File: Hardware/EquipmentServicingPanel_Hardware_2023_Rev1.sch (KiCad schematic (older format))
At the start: 42 parts, among them U1 Raspberry_Pi, U2 OKI, U3 TSR_1-2450

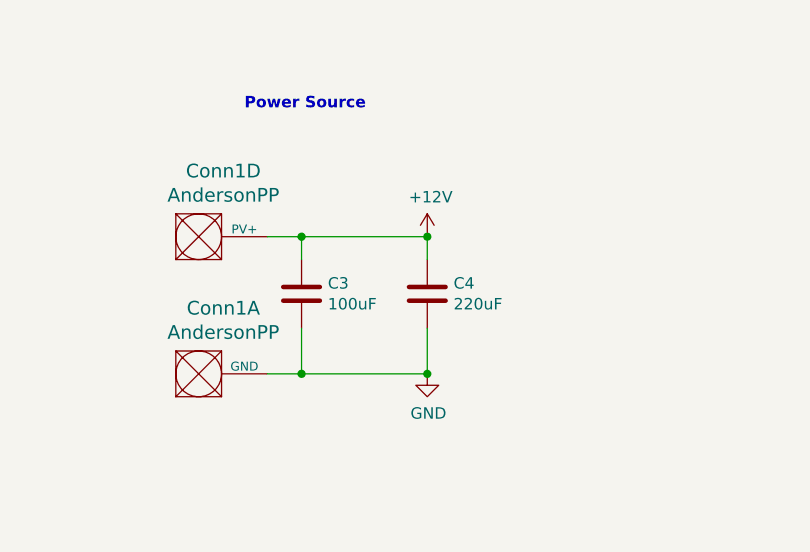
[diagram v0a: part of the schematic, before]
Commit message: Revert "Applied Kicad footprints"
This reverts commit d56fd15f2c9d233914814fde713dd6368af3c8bd.
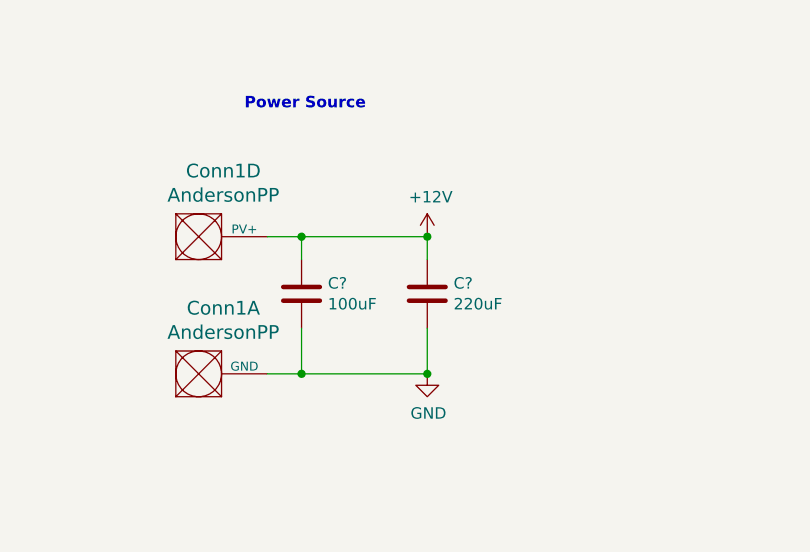
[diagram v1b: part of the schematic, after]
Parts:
- Conn1: footprint MRDT_Connectors:Square_Anderson_2_H_Stacked -> (none)
- Conn10, Conn11, Conn12, Conn13, Conn14, Conn15, Conn16, Conn17, Conn2, Conn3, Conn4, Conn5, Conn6, Conn7, Conn8, Conn9: footprint MRDT_Connectors:MOLEX_SL_02_Horizontal -> (none)
- renumbered C3 to C?, C4 to C?
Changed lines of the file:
@@
 F 0 "Conn2" H 2078 4658 60  0000 L CNN
 F 1 "Molex_SL_02" H 2078 4552 60  0000 L CNN
-F 2 "MRDT_Connectors:MOLEX_SL_02_Horizontal" H 1950 4400 60  0001 C CNN
+F 2 "" H 1950 4400 60  0001 C CNN
 F 3 "" H 1950 4400 60  0001 C CNN
 	1    1950 4500
@@
 F 0 "Conn3" H 3828 4658 60  0000 L CNN
 F 1 "Molex_SL_02" H 3828 4552 60  0000 L CNN
-F 2 "MRDT_Connectors:MOLEX_SL_02_Horizontal" H 3700 4400 60  0001 C CNN
+F 2 "" H 3700 4400 60  0001 C CNN
 F 3 "" H 3700 4400 60  0001 C CNN
 	1    3700 4500
@@
 F 0 "Conn4" H 3878 1508 60  0000 L CNN
 F 1 "Molex_SL_02" H 3878 1402 60  0000 L CNN
-F 2 "MRDT_Connectors:MOLEX_SL_02_Horizontal" H 3750 1250 60  0001 C CNN
+F 2 "" H 3750 1250 60  0001 C CNN
 F 3 "" H 3750 1250 60  0001 C CNN
 	1    3750 1350
@@
 F 0 "Conn7" H 4828 1508 60  0000 L CNN
 F 1 "Molex_SL_02" H 4828 1402 60  0000 L CNN
-F 2 "MRDT_Connectors:MOLEX_SL_02_Horizontal" H 4700 1250 60  0001 C CNN
+F 2 "" H 4700 1250 60  0001 C CNN
 F 3 "" H 4700 1250 60  0001 C CNN
 	1    4700 1350
@@
 F 0 "Conn1" H 1408 7537 60  0000 C CNN
 F 1 "AndersonPP" H 1408 7431 60  0000 C CNN
-F 2 "MRDT_Connectors:Square_Anderson_2_H_Stacked" H 1050 6600 60  0001 C CNN
+F 2 "" H 1050 6600 60  0001 C CNN
 F 3 "" H 1050 6600 60  0001 C CNN
 	1    1200 7150
@@
 F 0 "Conn1" H 1408 6937 60  0000 C CNN
 F 1 "AndersonPP" H 1408 6831 60  0000 C CNN
-F 2 "MRDT_Connectors:Square_Anderson_2_H_Stacked" H 1050 6000 60  0001 C CNN
+F 2 "" H 1050 6000 60  0001 C CNN
 F 3 "" H 1050 6000 60  0001 C CNN
 	4    1200 6550
@@
 F 0 "Conn5" H 4128 2358 60  0000 L CNN
 F 1 "Molex_SL_02" H 4128 2252 60  0000 L CNN
-F 2 "MRDT_Connectors:MOLEX_SL_02_Horizontal" H 4000 2100 60  0001 C CNN
+F 2 "" H 4000 2100 60  0001 C CNN
 F 3 "" H 4000 2100 60  0001 C CNN
 	1    4000 2200
@@
 F 0 "Conn6" H 4128 3008 60  0000 L CNN
 F 1 "Molex_SL_02" H 4128 2902 60  0000 L CNN
-F 2 "MRDT_Connectors:MOLEX_SL_02_Horizontal" H 4000 2750 60  0001 C CNN
+F 2 "" H 4000 2750 60  0001 C CNN
 F 3 "" H 4000 2750 60  0001 C CNN
 	1    4000 2850
@@
 F 0 "Conn8" H 5928 1458 60  0000 L CNN
 F 1 "Molex_SL_02" H 5928 1352 60  0000 L CNN
-F 2 "MRDT_Connectors:MOLEX_SL_02_Horizontal" H 5800 1200 60  0001 C CNN
+F 2 "" H 5800 1200 60  0001 C CNN
 F 3 "" H 5800 1200 60  0001 C CNN
 	1    5800 1300
@@
 F 0 "Conn9" H 5928 2008 60  0000 L CNN
 F 1 "Molex_SL_02" H 5928 1902 60  0000 L CNN
-F 2 "MRDT_Connectors:MOLEX_SL_02_Horizontal" H 5800 1750 60  0001 C CNN
+F 2 "" H 5800 1750 60  0001 C CNN
 F 3 "" H 5800 1750 60  0001 C CNN
 	1    5800 1850
@@
 F 0 "Conn11" H 6978 1458 60  0000 L CNN
 F 1 "Molex_SL_02" H 6978 1352 60  0000 L CNN
-F 2 "MRDT_Connectors:MOLEX_SL_02_Horizontal" H 6850 1200 60  0001 C CNN
+F 2 "" H 6850 1200 60  0001 C CNN
 F 3 "" H 6850 1200 60  0001 C CNN
 	1    6850 1300
@@
 F 0 "Conn12" H 6978 2008 60  0000 L CNN
 F 1 "Molex_SL_02" H 6978 1902 60  0000 L CNN
-F 2 "MRDT_Connectors:MOLEX_SL_02_Horizontal" H 6850 1750 60  0001 C CNN
+F 2 "" H 6850 1750 60  0001 C CNN
 F 3 "" H 6850 1750 60  0001 C CNN
 	1    6850 1850
@@
 F 0 "Conn13" H 6978 2608 60  0000 L CNN
 F 1 "Molex_SL_02" H 6978 2502 60  0000 L CNN
-F 2 "MRDT_Connectors:MOLEX_SL_02_Horizontal" H 6850 2350 60  0001 C CNN
+F 2 "" H 6850 2350 60  0001 C CNN
 F 3 "" H 6850 2350 60  0001 C CNN
 	1    6850 2450
@@
 F 0 "Conn10" H 5928 2608 60  0000 L CNN
 F 1 "Molex_SL_02" H 5928 2502 60  0000 L CNN
-F 2 "MRDT_Connectors:MOLEX_SL_02_Horizontal" H 5800 2350 60  0001 C CNN
+F 2 "" H 5800 2350 60  0001 C CNN
 F 3 "" H 5800 2350 60  0001 C CNN
 	1    5800 2450
@@
 F 0 "Conn14" H 9450 4100 60  0000 L CNN
 F 1 "Molex_SL_02" H 9400 3800 60  0000 L CNN
-F 2 "MRDT_Connectors:MOLEX_SL_02_Horizontal" H 9350 3800 60  0001 C CNN
+F 2 "" H 9350 3800 60  0001 C CNN
 F 3 "" H 9350 3800 60  0001 C CNN
 	1    9350 3900
@@
 F 0 "Conn16" H 10628 4058 60  0000 L CNN
 F 1 "Molex_SL_02" H 10628 3952 60  0000 L CNN
-F 2 "MRDT_Connectors:MOLEX_SL_02_Horizontal" H 10500 3800 60  0001 C CNN
+F 2 "" H 10500 3800 60  0001 C CNN
 F 3 "" H 10500 3800 60  0001 C CNN
 	1    10500 3900
@@
 F 0 "Conn17" H 10628 5208 60  0000 L CNN
 F 1 "Molex_SL_02" H 10628 5102 60  0000 L CNN
-F 2 "MRDT_Connectors:MOLEX_SL_02_Horizontal" H 10500 4950 60  0001 C CNN
+F 2 "" H 10500 4950 60  0001 C CNN
 F 3 "" H 10500 4950 60  0001 C CNN
 	1    10500 5050
@@
 F 0 "Conn15" H 9478 5208 60  0000 L CNN
 F 1 "Molex_SL_02" H 9200 5000 60  0000 L CNN
-F 2 "MRDT_Connectors:MOLEX_SL_02_Horizontal" H 9350 4950 60  0001 C CNN
+F 2 "" H 9350 4950 60  0001 C CNN
 F 3 "" H 9350 4950 60  0001 C CNN
 	1    9350 5050
@@
 	700  1500 1200 1500
 $Comp
-L Device:C C3
+L Device:C C?
 U 1 1 6437C966
 P 1750 6700
-F 0 "C3" H 1865 6746 50  0000 L CNN
+F 0 "C?" H 1865 6746 50  0000 L CNN
 F 1 "100uF" H 1865 6655 50  0000 L CNN
 F 2 "" H 1788 6550 50  0001 C CNN
@@
 $EndComp
 $Comp
-L Device:C C4
+L Device:C C?
 U 1 1 6437D77B
 P 2300 6700
-F 0 "C4" H 2415 6746 50  0000 L CNN
+F 0 "C?" H 2415 6746 50  0000 L CNN
 F 1 "220uF" H 2415 6655 50  0000 L CNN
 F 2 "" H 2338 6550 50  0001 C CNN

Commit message: Applied Kicad footprints
Applied Equipment Servicing footprints
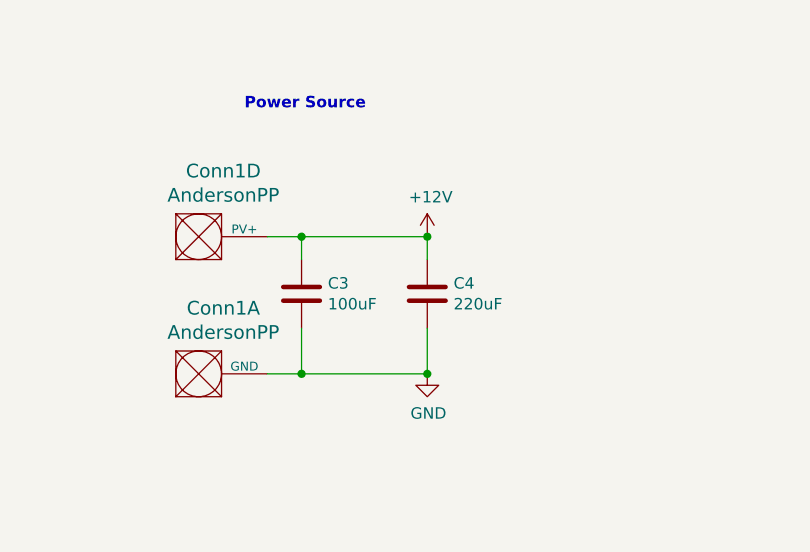
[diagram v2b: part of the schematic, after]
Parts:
- Conn1: footprint (none) -> MRDT_Connectors:Square_Anderson_2_H_Stacked
- Conn10, Conn11, Conn12, Conn13, Conn14, Conn15, Conn16, Conn17, Conn2, Conn3, Conn4, Conn5, Conn6, Conn7, Conn8, Conn9: footprint (none) -> MRDT_Connectors:MOLEX_SL_02_Horizontal
- gave numbers to parts that had none: 2
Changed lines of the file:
@@
 F 0 "Conn2" H 2078 4658 60  0000 L CNN
 F 1 "Molex_SL_02" H 2078 4552 60  0000 L CNN
-F 2 "" H 1950 4400 60  0001 C CNN
+F 2 "MRDT_Connectors:MOLEX_SL_02_Horizontal" H 1950 4400 60  0001 C CNN
 F 3 "" H 1950 4400 60  0001 C CNN
 	1    1950 4500
@@
 F 0 "Conn3" H 3828 4658 60  0000 L CNN
 F 1 "Molex_SL_02" H 3828 4552 60  0000 L CNN
-F 2 "" H 3700 4400 60  0001 C CNN
+F 2 "MRDT_Connectors:MOLEX_SL_02_Horizontal" H 3700 4400 60  0001 C CNN
 F 3 "" H 3700 4400 60  0001 C CNN
 	1    3700 4500
@@
 F 0 "Conn4" H 3878 1508 60  0000 L CNN
 F 1 "Molex_SL_02" H 3878 1402 60  0000 L CNN
-F 2 "" H 3750 1250 60  0001 C CNN
+F 2 "MRDT_Connectors:MOLEX_SL_02_Horizontal" H 3750 1250 60  0001 C CNN
 F 3 "" H 3750 1250 60  0001 C CNN
 	1    3750 1350
@@
 F 0 "Conn7" H 4828 1508 60  0000 L CNN
 F 1 "Molex_SL_02" H 4828 1402 60  0000 L CNN
-F 2 "" H 4700 1250 60  0001 C CNN
+F 2 "MRDT_Connectors:MOLEX_SL_02_Horizontal" H 4700 1250 60  0001 C CNN
 F 3 "" H 4700 1250 60  0001 C CNN
 	1    4700 1350
@@
 F 0 "Conn1" H 1408 7537 60  0000 C CNN
 F 1 "AndersonPP" H 1408 7431 60  0000 C CNN
-F 2 "" H 1050 6600 60  0001 C CNN
+F 2 "MRDT_Connectors:Square_Anderson_2_H_Stacked" H 1050 6600 60  0001 C CNN
 F 3 "" H 1050 6600 60  0001 C CNN
 	1    1200 7150
@@
 F 0 "Conn1" H 1408 6937 60  0000 C CNN
 F 1 "AndersonPP" H 1408 6831 60  0000 C CNN
-F 2 "" H 1050 6000 60  0001 C CNN
+F 2 "MRDT_Connectors:Square_Anderson_2_H_Stacked" H 1050 6000 60  0001 C CNN
 F 3 "" H 1050 6000 60  0001 C CNN
 	4    1200 6550
@@
 F 0 "Conn5" H 4128 2358 60  0000 L CNN
 F 1 "Molex_SL_02" H 4128 2252 60  0000 L CNN
-F 2 "" H 4000 2100 60  0001 C CNN
+F 2 "MRDT_Connectors:MOLEX_SL_02_Horizontal" H 4000 2100 60  0001 C CNN
 F 3 "" H 4000 2100 60  0001 C CNN
 	1    4000 2200
@@
 F 0 "Conn6" H 4128 3008 60  0000 L CNN
 F 1 "Molex_SL_02" H 4128 2902 60  0000 L CNN
-F 2 "" H 4000 2750 60  0001 C CNN
+F 2 "MRDT_Connectors:MOLEX_SL_02_Horizontal" H 4000 2750 60  0001 C CNN
 F 3 "" H 4000 2750 60  0001 C CNN
 	1    4000 2850
@@
 F 0 "Conn8" H 5928 1458 60  0000 L CNN
 F 1 "Molex_SL_02" H 5928 1352 60  0000 L CNN
-F 2 "" H 5800 1200 60  0001 C CNN
+F 2 "MRDT_Connectors:MOLEX_SL_02_Horizontal" H 5800 1200 60  0001 C CNN
 F 3 "" H 5800 1200 60  0001 C CNN
 	1    5800 1300
@@
 F 0 "Conn9" H 5928 2008 60  0000 L CNN
 F 1 "Molex_SL_02" H 5928 1902 60  0000 L CNN
-F 2 "" H 5800 1750 60  0001 C CNN
+F 2 "MRDT_Connectors:MOLEX_SL_02_Horizontal" H 5800 1750 60  0001 C CNN
 F 3 "" H 5800 1750 60  0001 C CNN
 	1    5800 1850
@@
 F 0 "Conn11" H 6978 1458 60  0000 L CNN
 F 1 "Molex_SL_02" H 6978 1352 60  0000 L CNN
-F 2 "" H 6850 1200 60  0001 C CNN
+F 2 "MRDT_Connectors:MOLEX_SL_02_Horizontal" H 6850 1200 60  0001 C CNN
 F 3 "" H 6850 1200 60  0001 C CNN
 	1    6850 1300
@@
 F 0 "Conn12" H 6978 2008 60  0000 L CNN
 F 1 "Molex_SL_02" H 6978 1902 60  0000 L CNN
-F 2 "" H 6850 1750 60  0001 C CNN
+F 2 "MRDT_Connectors:MOLEX_SL_02_Horizontal" H 6850 1750 60  0001 C CNN
 F 3 "" H 6850 1750 60  0001 C CNN
 	1    6850 1850
@@
 F 0 "Conn13" H 6978 2608 60  0000 L CNN
 F 1 "Molex_SL_02" H 6978 2502 60  0000 L CNN
-F 2 "" H 6850 2350 60  0001 C CNN
+F 2 "MRDT_Connectors:MOLEX_SL_02_Horizontal" H 6850 2350 60  0001 C CNN
 F 3 "" H 6850 2350 60  0001 C CNN
 	1    6850 2450
@@
 F 0 "Conn10" H 5928 2608 60  0000 L CNN
 F 1 "Molex_SL_02" H 5928 2502 60  0000 L CNN
-F 2 "" H 5800 2350 60  0001 C CNN
+F 2 "MRDT_Connectors:MOLEX_SL_02_Horizontal" H 5800 2350 60  0001 C CNN
 F 3 "" H 5800 2350 60  0001 C CNN
 	1    5800 2450
@@
 F 0 "Conn14" H 9450 4100 60  0000 L CNN
 F 1 "Molex_SL_02" H 9400 3800 60  0000 L CNN
-F 2 "" H 9350 3800 60  0001 C CNN
+F 2 "MRDT_Connectors:MOLEX_SL_02_Horizontal" H 9350 3800 60  0001 C CNN
 F 3 "" H 9350 3800 60  0001 C CNN
 	1    9350 3900
@@
 F 0 "Conn16" H 10628 4058 60  0000 L CNN
 F 1 "Molex_SL_02" H 10628 3952 60  0000 L CNN
-F 2 "" H 10500 3800 60  0001 C CNN
+F 2 "MRDT_Connectors:MOLEX_SL_02_Horizontal" H 10500 3800 60  0001 C CNN
 F 3 "" H 10500 3800 60  0001 C CNN
 	1    10500 3900
@@
 F 0 "Conn17" H 10628 5208 60  0000 L CNN
 F 1 "Molex_SL_02" H 10628 5102 60  0000 L CNN
-F 2 "" H 10500 4950 60  0001 C CNN
+F 2 "MRDT_Connectors:MOLEX_SL_02_Horizontal" H 10500 4950 60  0001 C CNN
 F 3 "" H 10500 4950 60  0001 C CNN
 	1    10500 5050
@@
 F 0 "Conn15" H 9478 5208 60  0000 L CNN
 F 1 "Molex_SL_02" H 9200 5000 60  0000 L CNN
-F 2 "" H 9350 4950 60  0001 C CNN
+F 2 "MRDT_Connectors:MOLEX_SL_02_Horizontal" H 9350 4950 60  0001 C CNN
 F 3 "" H 9350 4950 60  0001 C CNN
 	1    9350 5050
@@
 	700  1500 1200 1500
 $Comp
-L Device:C C?
+L Device:C C3
 U 1 1 6437C966
 P 1750 6700
-F 0 "C?" H 1865 6746 50  0000 L CNN
+F 0 "C3" H 1865 6746 50  0000 L CNN
 F 1 "100uF" H 1865 6655 50  0000 L CNN
 F 2 "" H 1788 6550 50  0001 C CNN
@@
 $EndComp
 $Comp
-L Device:C C?
+L Device:C C4
 U 1 1 6437D77B
 P 2300 6700
-F 0 "C?" H 2415 6746 50  0000 L CNN
+F 0 "C4" H 2415 6746 50  0000 L CNN
 F 1 "220uF" H 2415 6655 50  0000 L CNN
 F 2 "" H 2338 6550 50  0001 C CNN
